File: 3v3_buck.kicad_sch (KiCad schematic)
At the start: 11 parts, among them U1101 TLV62569DBVR

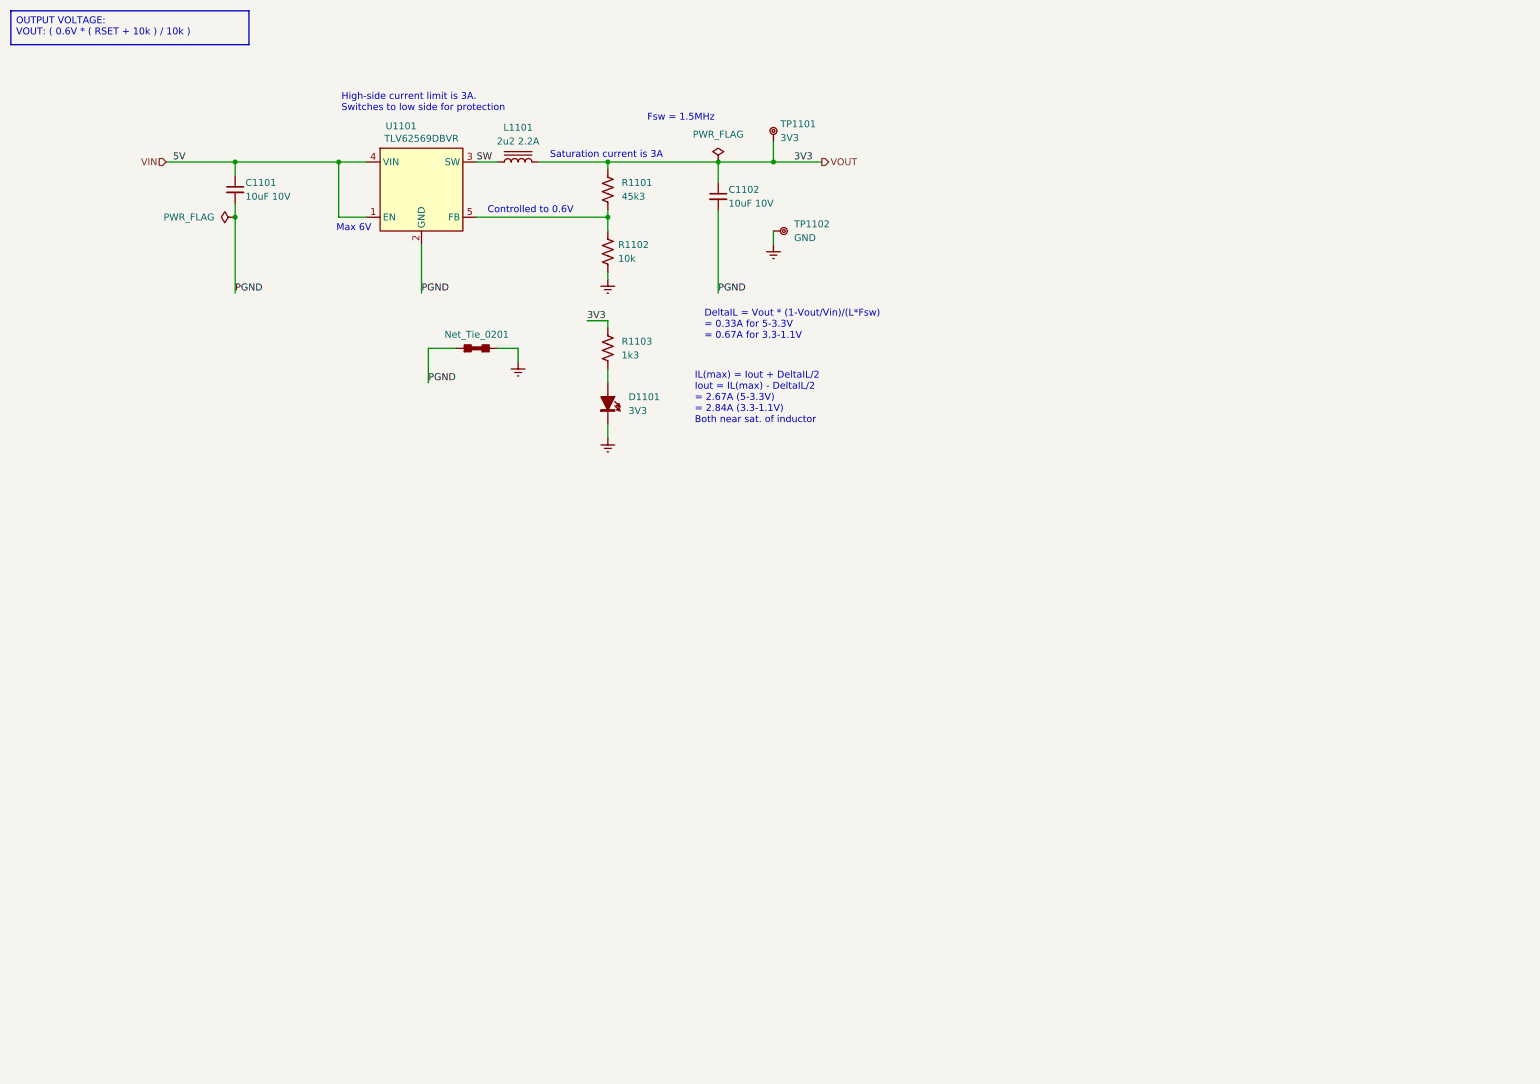
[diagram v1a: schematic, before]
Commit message: switching dcdc
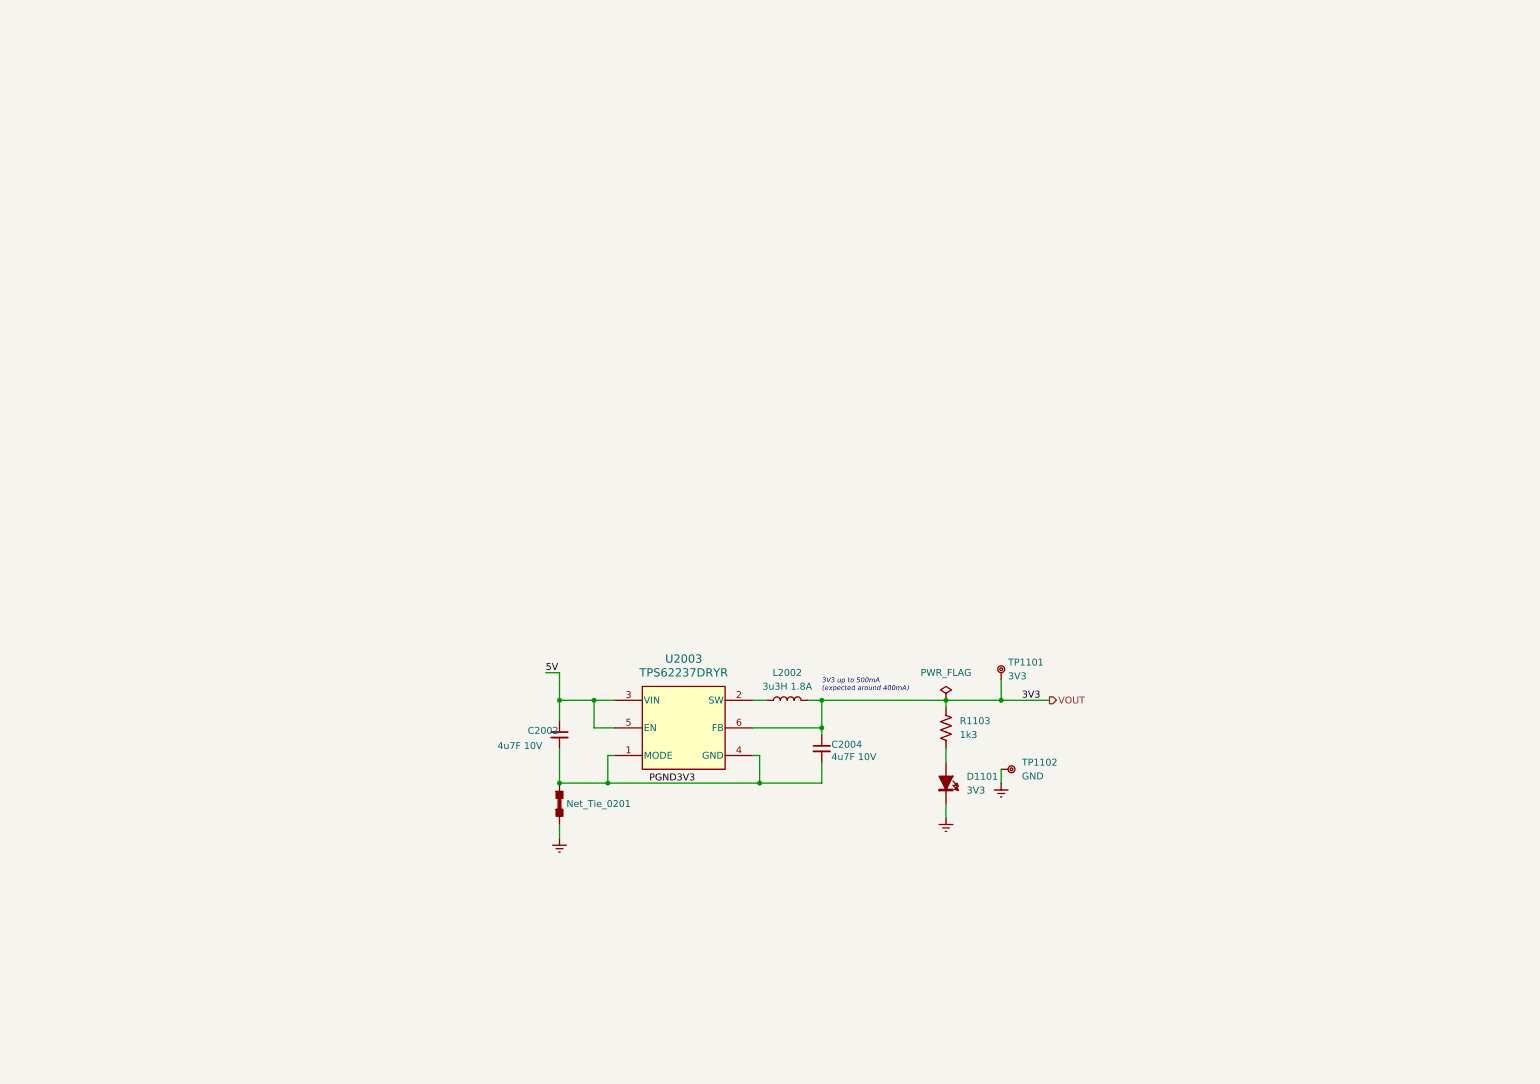
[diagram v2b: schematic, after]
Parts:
- removed C1101, C1102: 10uF 10V, BR_Passives:C_0402_1005Metric-minimized, symbol BR_Capacitors_0402:C_0402_10uF_10V_X5R_20%
- removed L1101: 2u2 2.2A, BR_Inductors:L_Taiyo-Yuden_NR-4018, symbol BR_Inductors:L_NRS4018T2R2MDGJV
- removed NT1101: Net_Tie_0201, BR_Virtual_Parts:Net_Tie_0201_1608Metric, symbol BR_Virtual_Parts:Net_Tie_0201
- removed R1101: 45k3, BR_Passives:C_0402_1005Metric-minimized, symbol BR_Resistors_0402:R_0402_45k3
- removed R1102: 10k, BR_Passives:R_0201_0603Metric-minimized, symbol BR_Resistors_0201:R_0201_10k
- removed U1101: TLV62569DBVR, BR_SOT:SOT-23-5_mini, symbol BR_IC_Regulators:TLV62569DBVR
- added C2002, C2004: 4u7F 10V, BR_Passives:C_0402_1005Metric-minimized, symbol BR_Capacitors_0402:C_0402_4u7F_10V_X7T_20%
- added L2002: 3u3H 1.8A, BR_Inductors:L_0805_2012Metric_Minimized, symbol BR_Inductors:L_XRTC201212S3R3MBCA
- added NT1102: Net_Tie_0201, BR_Virtual_Parts:Net_Tie_0201_1608Metric, symbol BR_Virtual_Parts:Net_Tie_0201
- added U2003: TPS62237DRYR, BR_SON:USON-6_1x1.45mm_P0.5mm, symbol BR_IC_Regulators:TPS62237DRYR
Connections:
- net GND: now also NT1102.2
- net VOUT: now also C2004.1, L2002.2, U2003.6 (FB)
- new net: L2002.1, U2003.2 (SW)
- new net 5V: C2002.1, U2003.3 (VIN), U2003.5 (EN)
- new net PGND3V3: C2002.2, C2004.2, NT1102.1, U2003.1 (MODE), U2003.4 (GND)
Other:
- note added: "3V3 up to 500mA (expected around 400mA)"
- note removed: "Controlled to 0.6V"
- note removed: "DeltaIL = Vout * (1-Vout/Vin)/(L*Fsw) = 0.33A for 5-3.3V = 0.67A for 3.3-1.1V"
- note removed: "Fsw = 1.5MHz"
- note removed: "High-side current limit is 3A. Switches to low side for protection"
- note removed: "IL(max) = Iout + DeltaIL/2 Iout = IL(max) - DeltaIL/2 = 2.67A (5-3.3V) = 2.84A (3.3-1.1V) Both near sat. of inductor"
- note removed: "Max 6V"
- note removed: "Saturation current is 3A"
- moved on the sheet: D1101, R1103, TP1101, TP1102

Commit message: more
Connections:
- net 5V renamed VIN
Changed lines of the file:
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@@
+		)
+	)
+	(hierarchical_label "VIN"
+		(shape input)
+		(at 146.05 171.45 180)
+		(effects
+			(font
+				(size 1.27 1.27)
+			)
+			(justify right)
 		)
 	)
 	(hierarchical_label "VOUT"
-		(shape output)
+		(shape input)
 		(at 236.22 171.45 0)
 		(effects

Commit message: more work
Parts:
- removed NT1102: Net_Tie_0201, BR_Virtual_Parts:Net_Tie_0201_1608Metric, symbol BR_Virtual_Parts:Net_Tie_0201
- added NT1101: Net_Tie_0201, BR_Virtual_Parts:Net_Tie_0201_1608Metric, symbol BR_Virtual_Parts:Net_Tie_0201
- C2002, C2004: JLCPCB Part Num (none) -> C20044522
- L2002: JLCPCB Part Num (none) -> C39846694
- TP1101: value 3V3 -> TP_RING_TH
- TP1102: value GND -> TP_RING_TH
- U2003: JLCPCB Part Num (none) -> C398923
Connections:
- net GND: now also NT1101.2
- net PGND3V3 renamed PGND
- net PGND: now also NT1101.1
- net VOUT renamed 3V3
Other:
- note added: "5V Input"
- moved on the sheet: D1101, TP1101

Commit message: more work
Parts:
- renumbered C2002 to C1101, C2004 to C1102, L2002 to L1101, R1103 to R1101, U2003 to U1101
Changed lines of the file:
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@@
 		(dnp no)
 		(fields_autoplaced yes)
-		(property "Reference" "R1103"
+		(property "Reference" "R1101"
 			(at 219.71 175.2599 0)
 			(show_name no)
@@
 			(project "PingDevKit"
 				(path "/2a5ce3ef-537a-4122-a1be-ef76186bc0d7/774f2c6c-c15c-4713-acf0-4edb2ec6be20/04bd0704-dffb-4d19-a31b-74299529bdb7"
-					(reference "R1103")
+					(reference "R1101")
 					(unit 1)
 				)
@@
 		(dnp no)
 		(fields_autoplaced yes)
-		(property "Reference" "U2003"
+		(property "Reference" "U1101"
 			(at 168.91 163.83 0)
 			(show_name no)
@@
 			(project "PingDevKit"
 				(path "/2a5ce3ef-537a-4122-a1be-ef76186bc0d7/774f2c6c-c15c-4713-acf0-4edb2ec6be20/04bd0704-dffb-4d19-a31b-74299529bdb7"
-					(reference "U2003")
+					(reference "U1101")
 					(unit 1)
 				)
@@
 		(in_pos_files yes)
 		(dnp no)
-		(property "Reference" "#PWR01107"
+		(property "Reference" "#PWR01104"
 			(at 146.05 170.18 0)
 			(hide yes)
@@
 			(project "PingDevKit"
 				(path "/2a5ce3ef-537a-4122-a1be-ef76186bc0d7/774f2c6c-c15c-4713-acf0-4edb2ec6be20/04bd0704-dffb-4d19-a31b-74299529bdb7"
-					(reference "#PWR01107")
+					(reference "#PWR01104")
 					(unit 1)
 				)
@@
 		(in_pos_files no)
 		(dnp no)
-		(property "Reference" "#PWR01109"
+		(property "Reference" "#PWR01108"
 			(at 181.61 212.09 0)
 			(hide yes)
@@
 			(project "PingDevKit"
 				(path "/2a5ce3ef-537a-4122-a1be-ef76186bc0d7/774f2c6c-c15c-4713-acf0-4edb2ec6be20/04bd0704-dffb-4d19-a31b-74299529bdb7"
-					(reference "#PWR01109")
+					(reference "#PWR01108")
 					(unit 1)
 				)
@@
 		(in_pos_files no)
 		(dnp no)
-		(property "Reference" "#PWR01105"
+		(property "Reference" "#PWR01107"
 			(at 165.1 212.09 0)
 			(hide yes)
@@
 			(project "PingDevKit"
 				(path "/2a5ce3ef-537a-4122-a1be-ef76186bc0d7/774f2c6c-c15c-4713-acf0-4edb2ec6be20/04bd0704-dffb-4d19-a31b-74299529bdb7"
-					(reference "#PWR01105")
+					(reference "#PWR01107")
 					(unit 1)
 				)
@@
 		(in_pos_files no)
 		(dnp no)
-		(property "Reference" "#PWR01108"
+		(property "Reference" "#PWR01105"
 			(at 146.05 193.04 0)
 			(hide yes)
@@
 			(project "PingDevKit"
 				(path "/2a5ce3ef-537a-4122-a1be-ef76186bc0d7/774f2c6c-c15c-4713-acf0-4edb2ec6be20/04bd0704-dffb-4d19-a31b-74299529bdb7"
-					(reference "#PWR01108")
+					(reference "#PWR01105")
 					(unit 1)
 				)
@@
 		(in_pos_files no)
 		(dnp no)
-		(property "Reference" "#PWR01113"
+		(property "Reference" "#PWR01111"
 			(at 217.17 193.04 0)
 			(hide yes)
@@
 			(project "PingDevKit"
 				(path "/2a5ce3ef-537a-4122-a1be-ef76186bc0d7/774f2c6c-c15c-4713-acf0-4edb2ec6be20/04bd0704-dffb-4d19-a31b-74299529bdb7"
-					(reference "#PWR01113")
+					(reference "#PWR01111")
 					(unit 1)
 				)
@@
 		(in_pos_files no)
 		(dnp no)
-		(property "Reference" "#PWR01103"
+		(property "Reference" "#PWR01113"
 			(at 227.33 193.04 0)
 			(hide yes)
@@
 			(project "PingDevKit"
 				(path "/2a5ce3ef-537a-4122-a1be-ef76186bc0d7/774f2c6c-c15c-4713-acf0-4edb2ec6be20/04bd0704-dffb-4d19-a31b-74299529bdb7"
-					(reference "#PWR01103")
+					(reference "#PWR01113")
 					(unit 1)
 				)
@@
 		(in_pos_files no)
 		(dnp no)
-		(property "Reference" "#PWR01110"
+		(property "Reference" "#PWR01106"
 			(at 154.94 193.04 0)
 			(hide yes)
@@
 			(project "PingDevKit"
 				(path "/2a5ce3ef-537a-4122-a1be-ef76186bc0d7/774f2c6c-c15c-4713-acf0-4edb2ec6be20/04bd0704-dffb-4d19-a31b-74299529bdb7"
-					(reference "#PWR01110")
+					(reference "#PWR01106")
 					(unit 1)
 				)
@@
 		(in_pos_files no)
 		(dnp no)
-		(property "Reference" "#PWR01112"
+		(property "Reference" "#PWR01110"
 			(at 194.31 193.04 0)
 			(hide yes)
@@
 			(project "PingDevKit"
 				(path "/2a5ce3ef-537a-4122-a1be-ef76186bc0d7/774f2c6c-c15c-4713-acf0-4edb2ec6be20/04bd0704-dffb-4d19-a31b-74299529bdb7"
-					(reference "#PWR01112")
+					(reference "#PWR01110")
 					(unit 1)
 				)
@@
 		(dnp no)
 		(fields_autoplaced yes)
-		(property "Reference" "L2002"
+		(property "Reference" "L1101"
 			(at 187.96 166.37 90)
 			(show_name no)
@@
 			(project "PingDevKit"
 				(path "/2a5ce3ef-537a-4122-a1be-ef76186bc0d7/774f2c6c-c15c-4713-acf0-4edb2ec6be20/04bd0704-dffb-4d19-a31b-74299529bdb7"
-					(reference "L2002")
+					(reference "L1101")
 					(unit 1)
 				)
@@
 		(in_pos_files yes)
 		(dnp no)
-		(property "Reference" "#PWR01106"
+		(property "Reference" "#PWR01103"
 			(at 107.95 162.56 0)
 			(hide yes)
@@
 			(project "PingDevKit"
 				(path "/2a5ce3ef-537a-4122-a1be-ef76186bc0d7/774f2c6c-c15c-4713-acf0-4edb2ec6be20/04bd0704-dffb-4d19-a31b-74299529bdb7"
-					(reference "#PWR01106")
+					(reference "#PWR01103")
 					(unit 1)
 				)
@@
 		(in_pos_files yes)
 		(dnp no)
-		(property "Reference" "C2004"
+		(property "Reference" "C1102"
 			(at 196.088 179.578 0)
 			(show_name no)
@@
 			(project "PingDevKit"
 				(path "/2a5ce3ef-537a-4122-a1be-ef76186bc0d7/774f2c6c-c15c-4713-acf0-4edb2ec6be20/04bd0704-dffb-4d19-a31b-74299529bdb7"
-					(reference "C2004")
+					(reference "C1102")
 					(unit 1)
 				)
@@
 		(in_pos_files yes)
 		(dnp no)
-		(property "Reference" "#PWR01104"
+		(property "Reference" "#PWR01112"
 			(at 224.79 175.26 0)
 			(hide yes)
@@
 			(project "PingDevKit"
 				(path "/2a5ce3ef-537a-4122-a1be-ef76186bc0d7/774f2c6c-c15c-4713-acf0-4edb2ec6be20/04bd0704-dffb-4d19-a31b-74299529bdb7"
-					(reference "#PWR01104")
+					(reference "#PWR01112")
 					(unit 1)
 				)
@@
 		(in_pos_files yes)
 		(dnp no)
-		(property "Reference" "C2002"
+		(property "Reference" "C1101"
 			(at 140.208 177.038 0)
 			(show_name no)
@@
 			(project "PingDevKit"
 				(path "/2a5ce3ef-537a-4122-a1be-ef76186bc0d7/774f2c6c-c15c-4713-acf0-4edb2ec6be20/04bd0704-dffb-4d19-a31b-74299529bdb7"
-					(reference "C2002")
+					(reference "C1101")
 					(unit 1)
 				)
@@
 		(in_pos_files no)
 		(dnp no)
-		(property "Reference" "#PWR01111"
+		(property "Reference" "#PWR01109"
 			(at 182.88 193.04 0)
 			(hide yes)
@@
 			(project "PingDevKit"
 				(path "/2a5ce3ef-537a-4122-a1be-ef76186bc0d7/774f2c6c-c15c-4713-acf0-4edb2ec6be20/04bd0704-dffb-4d19-a31b-74299529bdb7"
-					(reference "#PWR01111")
+					(reference "#PWR01109")
 					(unit 1)
 				)

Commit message: work
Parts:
- removed TP1101, TP1102: TP_RING_TH, BR_Connectors:TEST-TH_BD2.54-P1.4_RED, symbol BR_Connectors:TP_Ring_PTH
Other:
- moved on the sheet: C1101, C1102, D1101, L1101, R1101, U1101

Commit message: getting really close to final
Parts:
- R1101: footprint BR_Passives:C_0402_1005Metric-minimized -> BR_Passives:R_0402_1005Metric-minimized
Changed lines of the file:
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@@
 			)
 		)
-		(property "Footprint" "BR_Passives:C_0402_1005Metric-minimized"
+		(property "Footprint" "BR_Passives:R_0402_1005Metric-minimized"
 			(at 313.69 129.54 0)
 			(hide yes)
